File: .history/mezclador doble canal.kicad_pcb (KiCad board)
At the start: 2 copper layers, 54.4 x 61.3 mm, 31 parts, among them J1 Conn_Coaxial, J2 Conn_Coaxial, J3 Conn_Coaxial, J4 Conn_Coaxial, J5 Conn_Coaxial, J6 Conn_Coaxial, J7 Screw_Terminal_01x02, U1 NE5532

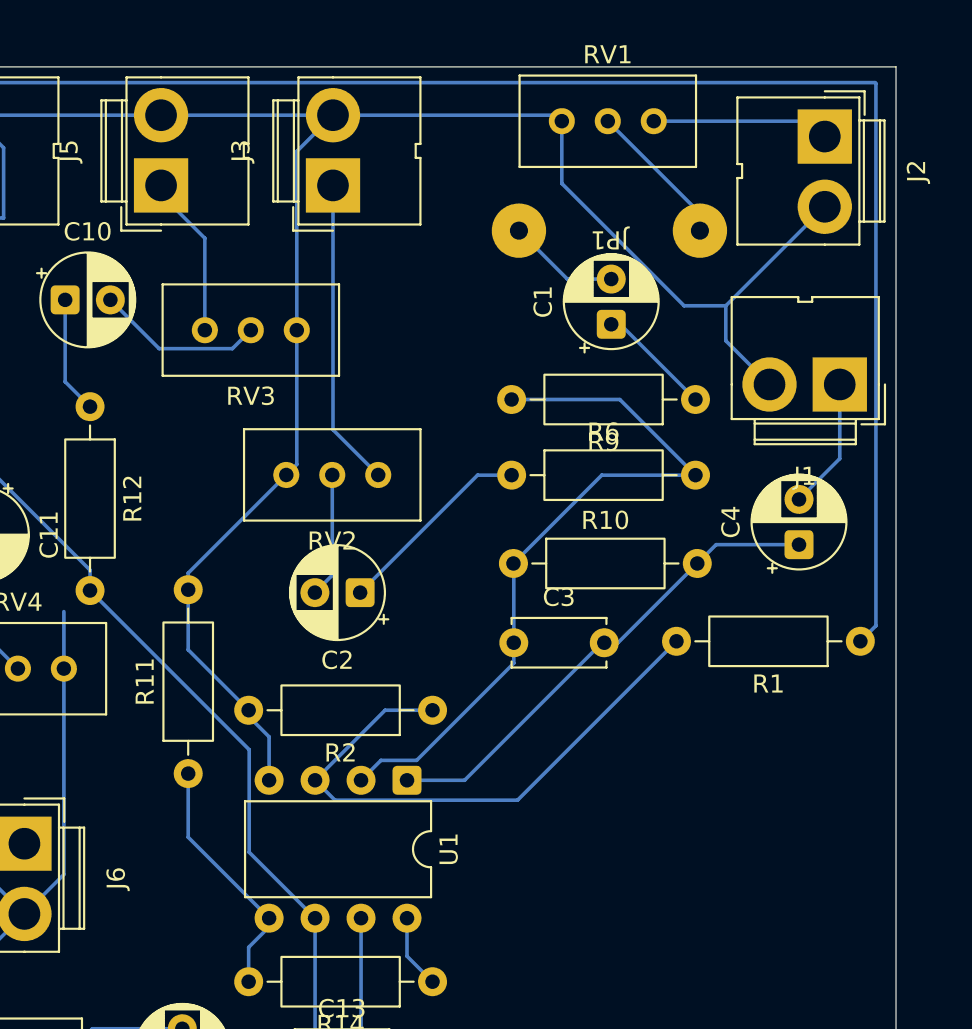
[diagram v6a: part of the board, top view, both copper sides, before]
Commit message: agregando pads potenciometros
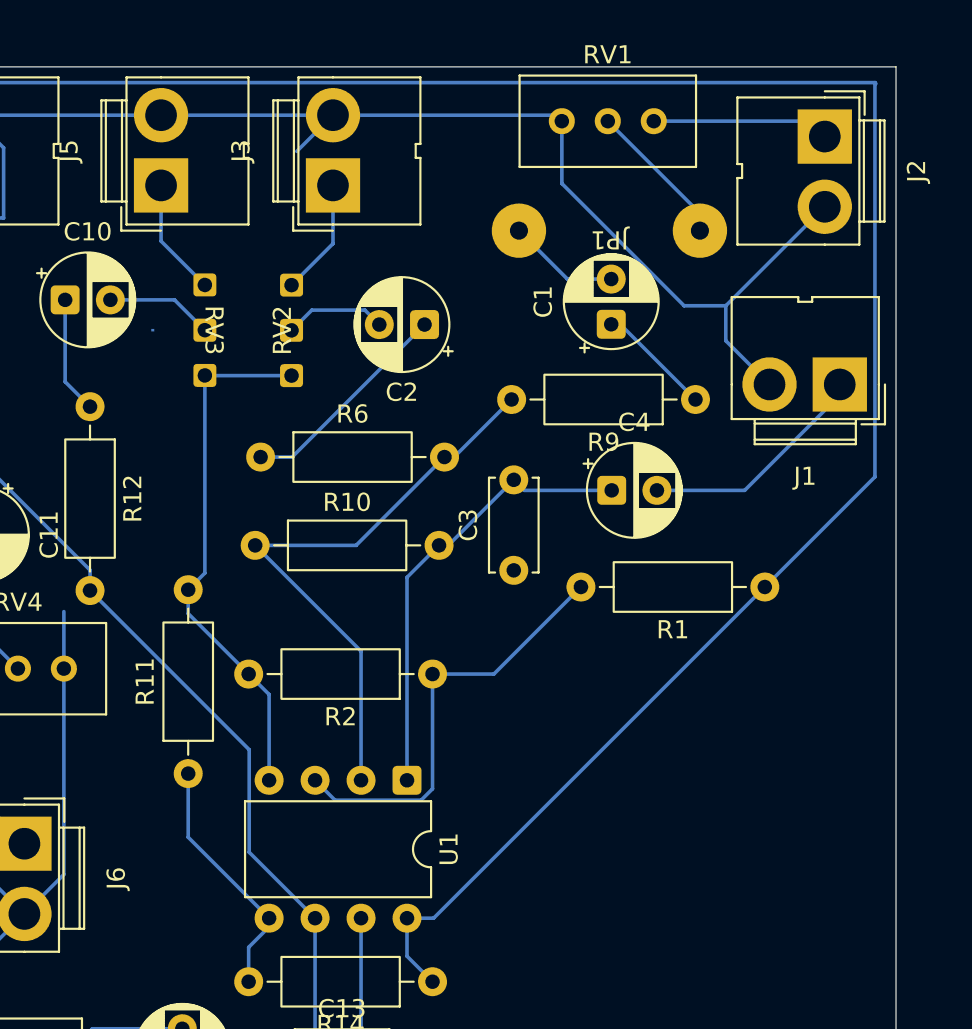
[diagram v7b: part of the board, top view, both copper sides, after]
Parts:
- RV2, RV3: footprint Potentiometer_THT:Potentiometer_Bourns_3296W_Vertical -> personal:potentiometer pads
- moved C2 15.2 mm to (201.6, 58.2)
- moved R10 14.3 mm to (192.2, 70.4)
- moved R6 13.9 mm to (192.5, 65.5)
- moved C4 10.8 mm to (211.9, 67.3), turned to 0 degrees
- moved RV2 8.00 mm to (194.2, 58.5), turned to 90 degrees
- moved R1 6.07 mm to (220.4, 72.7)
- moved C3 4.00 mm to (206.5, 71.8), turned to 90 degrees
- moved R2 2.00 mm to (202.0, 77.5)
- turned RV3 to -90 degrees
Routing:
- net VCC: track 92.9 -> 119.5 mm
- net Net-(J3-In): track 17.0 -> 6.46 mm
- net GND: track 177.4 -> 167.7 mm
- net Net-(U1A-+): track 32.2 -> 23.7 mm
- net Net-(U1A--): track 40.6 -> 32.9 mm
- net Net-(J1-In): track 7.28 -> 12.9 mm
- net Net-(C10-Pad2): track 9.30 -> 5.91 mm
- net Net-(C3-Pad2): track 27.5 -> 25.0 mm
- net Net-(J5-In): track 9.00 -> 6.50 mm
- net Net-(C2-Pad2): track 6.90 -> 5.65 mm
- net Net-(C2-Pad1): track 11.1 -> 12.1 mm

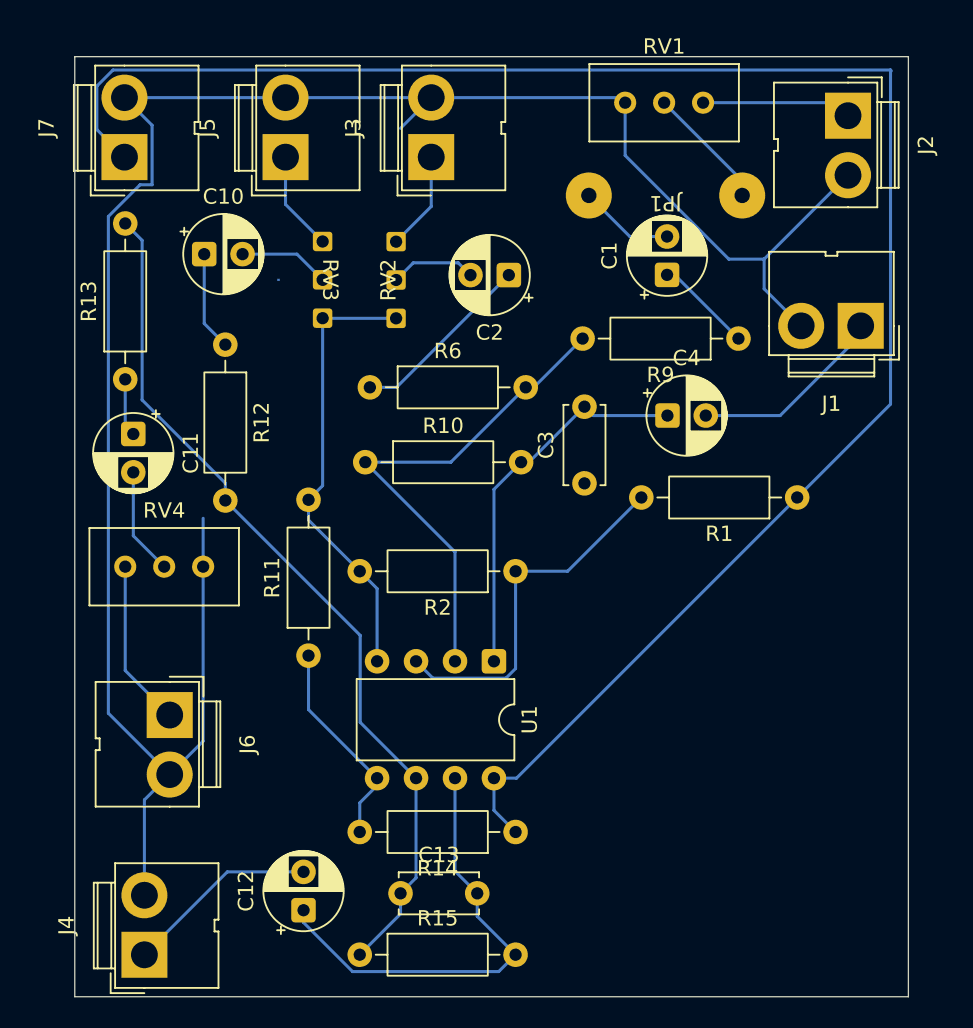
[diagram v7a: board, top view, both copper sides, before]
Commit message: mejorando distribucion de componentes
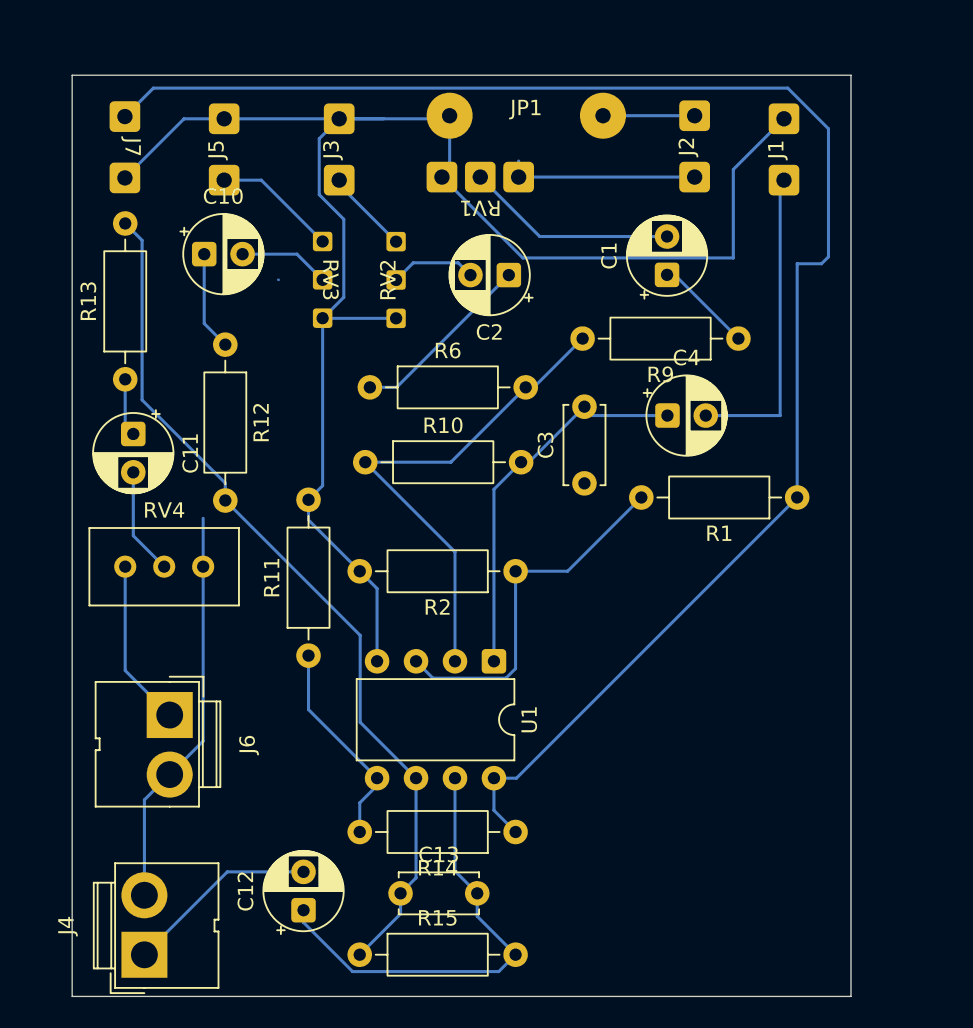
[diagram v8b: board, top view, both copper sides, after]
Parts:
- J1, J2, J3, J5, J7: footprint Connector:JWT_A3963_1x02_P3.96mm_Vertical -> personal:double wire
- JP1: value Jumper_2_Open -> Jumper_2_Bridged
- RV1: footprint Potentiometer_THT:Potentiometer_Bourns_3296W_Vertical -> personal:potentiometer pads
- moved RV1 15.3 mm to (199.7, 51.8), turned to 180 degrees
- moved J1 12.5 mm to (219.5, 50.0), turned to 90 degrees
- moved JP1 10.5 mm to (202.7, 47.8), turned to 0 degrees
- moved J2 10.2 mm to (213.7, 49.8), turned to 90 degrees
- moved J3 6.02 mm to (190.5, 50.0)
- moved J5 4.03 mm to (183.0, 50.0)
- moved J7 0.65 mm to (176.5, 49.9), turned to -90 degrees
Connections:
- C1 pad 2: Net-(JP1-B) -> Net-(C1-Pad2)
- J2 pad 2: GND -> Net-(J2-Ext)
- JP1 pad 1: Net-(JP1-A) -> GND
- JP1 pad 2: Net-(JP1-B) -> Net-(J2-Ext)
- RV1 pad 2: Net-(JP1-A) -> Net-(C1-Pad2)
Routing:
- net GND: track 167.7 -> 131.9 mm
- net VCC: track 119.5 -> 105.0 mm
- net Net-(C1-Pad2): track 0.00 -> 13.8 mm
- net Net-(JP1-A): track 8.16 -> 0.00 mm
- net Net-(J1-In): track 12.9 -> 20.3 mm
- net Net-(JP1-B): track 6.21 -> 0.00 mm
- net Net-(J2-Ext): track 0.00 -> 5.98 mm
- net Net-(J2-In): track 10.0 -> 12.5 mm
- net Net-(J5-In): track 6.50 -> 8.08 mm
- net Net-(J3-In): track 6.46 -> 5.55 mm
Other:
- board size 54.4 x 61.3 mm -> 50.8 x 60.1 mm
